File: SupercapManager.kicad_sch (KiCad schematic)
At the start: 9 parts, among them J1 JST4_F, J2 XT30_F, J3 XT30_F, J4 XT30_F, J5 XT30_F, Q11 BSC059N04LS6, Q12 BSC059N04LS6

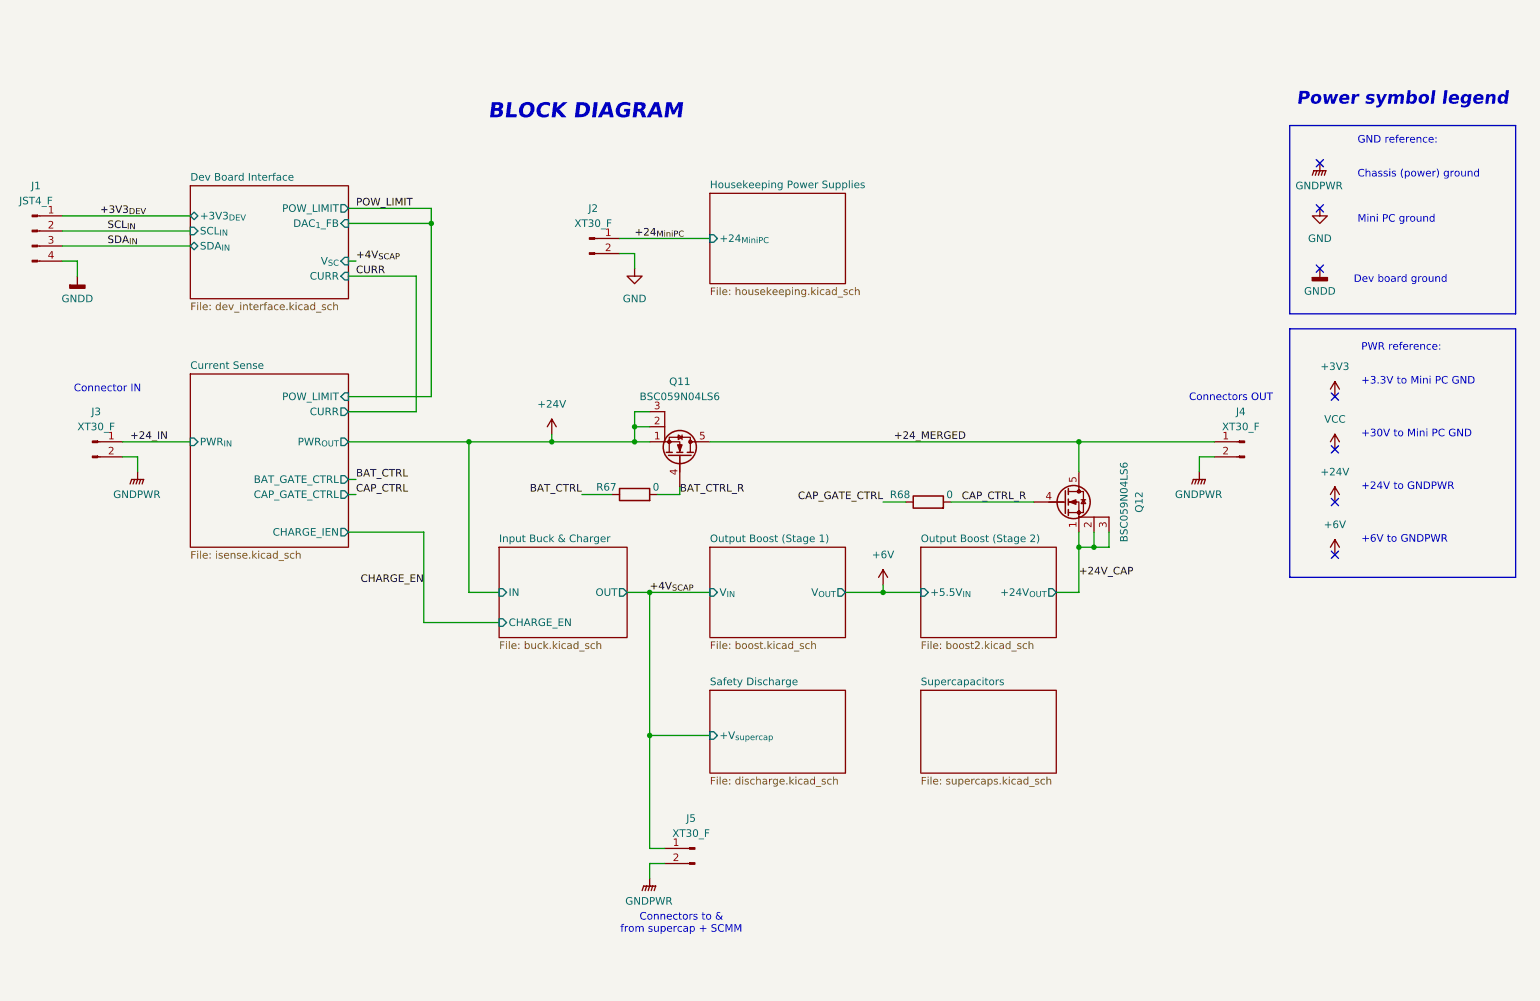
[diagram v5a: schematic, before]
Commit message: Adding simulation for charging & balancing
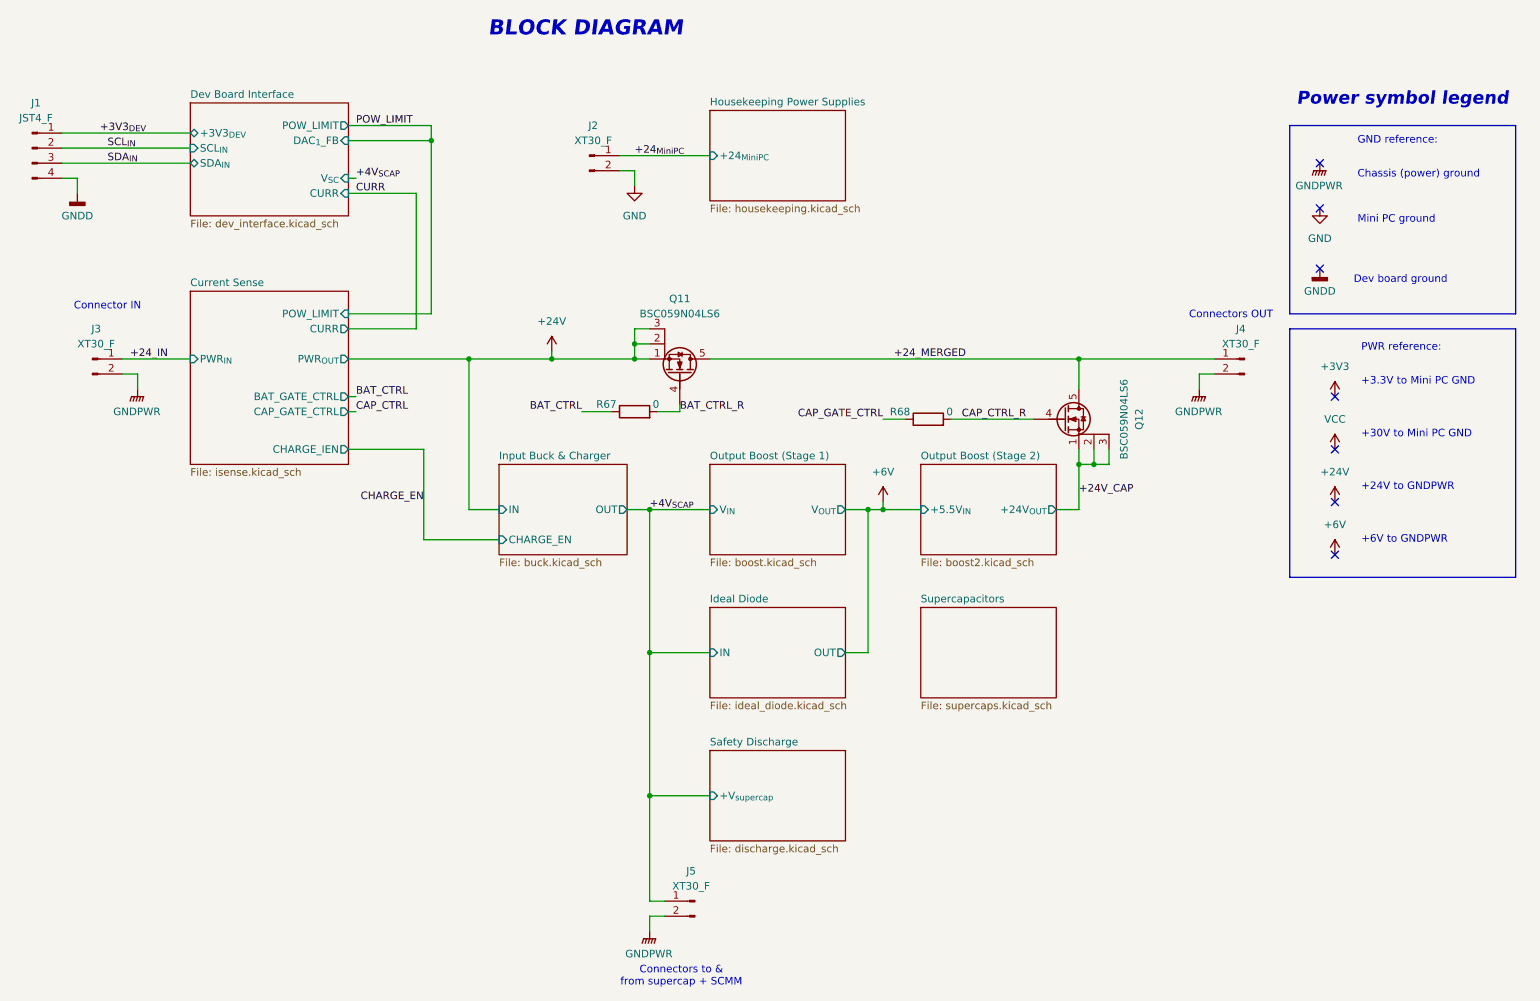
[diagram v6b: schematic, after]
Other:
- added sheet Ideal Diode (ideal_diode.kicad_sch)
- moved on the sheet: J1, J2, J3, J4, J5, Q11, Q12, R67, R68

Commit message: Various schematic touchups
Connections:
- net +4V_{SCAP}: no longer J5.1 (Pin_1)
- new net +6V_{SCAP}: J5.1 (Pin_1)
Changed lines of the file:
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@@
-	)
-	(junction
-		(at 165.1 105.41)
-		(diameter 0)
-		(color 0 0 0 0)
 	)
 	(junction
@@
 	(wire
 		(pts
-			(xy 165.1 105.41) (xy 171.45 105.41)
+			(xy 162.56 105.41) (xy 171.45 105.41)
 		)
 		(stroke
@@
 	(wire
 		(pts
-			(xy 162.56 105.41) (xy 165.1 105.41)
-		)
-		(stroke
-			(width 0)
-			(type default)
-		)
-	)
-	(wire
-		(pts
 			(xy 95.25 105.41) (xy 100.33 105.41)
 		)
@@
 		(pts
 			(xy 198.12 85.09) (xy 198.12 80.01)
-		)
-		(stroke
-			(width 0)
-			(type default)
-		)
-	)
-	(wire
-		(pts
-			(xy 165.1 104.14) (xy 165.1 105.41)
 		)
 		(stroke
@@
 		)
 	)
+	(label "+4.4V_{SCAP}"
+		(at 160.02 105.41 0)
+		(effects
+			(font
+				(size 1.27 1.27)
+			)
+			(justify left bottom)
+		)
+	)
 	(label "+24_{MiniPC}"
 		(at 123.19 45.72 0)
@@
 		)
 	)
-	(label "+4V_{SCAP}"
+	(label "+6V_{SCAP}"
 		(at 125.73 105.41 0)
 		(effects
@@
 					(unit 1)
 				)
-			)
-		)
-	)
-	(symbol
-		(lib_id "power:+6V")
-		(at 165.1 104.14 0)
-		(unit 1)
-		(exclude_from_sim no)
-		(in_bom yes)
-		(on_board yes)
-		(dnp no)
-		(fields_autoplaced yes)
-		(property "Reference" "#PWR020"
-			(at 165.1 107.95 0)
-			(effects
-				(font
-					(size 1.27 1.27)
-				)
-				(hide yes)
-			)
-		)
-		(property "Value" "+6V"
-			(at 165.1 99.06 0)
-			(effects
-				(font
-					(size 1.27 1.27)
-				)
-			)
-		)
-		(property "Footprint" ""
-			(at 165.1 104.14 0)
-			(effects
-				(font
-					(size 1.27 1.27)
-				)
-				(hide yes)
-			)
-		)
-		(property "Datasheet" ""
-			(at 165.1 104.14 0)
-			(effects
-				(font
-					(size 1.27 1.27)
-				)
-				(hide yes)
-			)
-		)
-		(property "Description" "Power symbol creates a global label with name \"+6V\""
-			(at 165.1 104.14 0)
-			(effects
-				(font
-					(size 1.27 1.27)
-				)
-				(hide yes)
-			)
-		)
-		(pin "1"
-		)
-		(instances
-			(project ""
-				(path "/6197145b-e7d4-44cc-9d90-537b6501bf60"
-					(reference "#PWR020")
-					(unit 1)
-				)
